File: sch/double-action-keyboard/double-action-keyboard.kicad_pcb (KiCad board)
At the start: 2 copper layers, 134 x 90 mm, 147 parts, among them J1 Conn_01x02, J2 Conn_01x04, J3 Conn_01x04, U1 Pico, U2 AQM1602XA-RN-GBW, U3 AQM1602Y-NLW-FBW

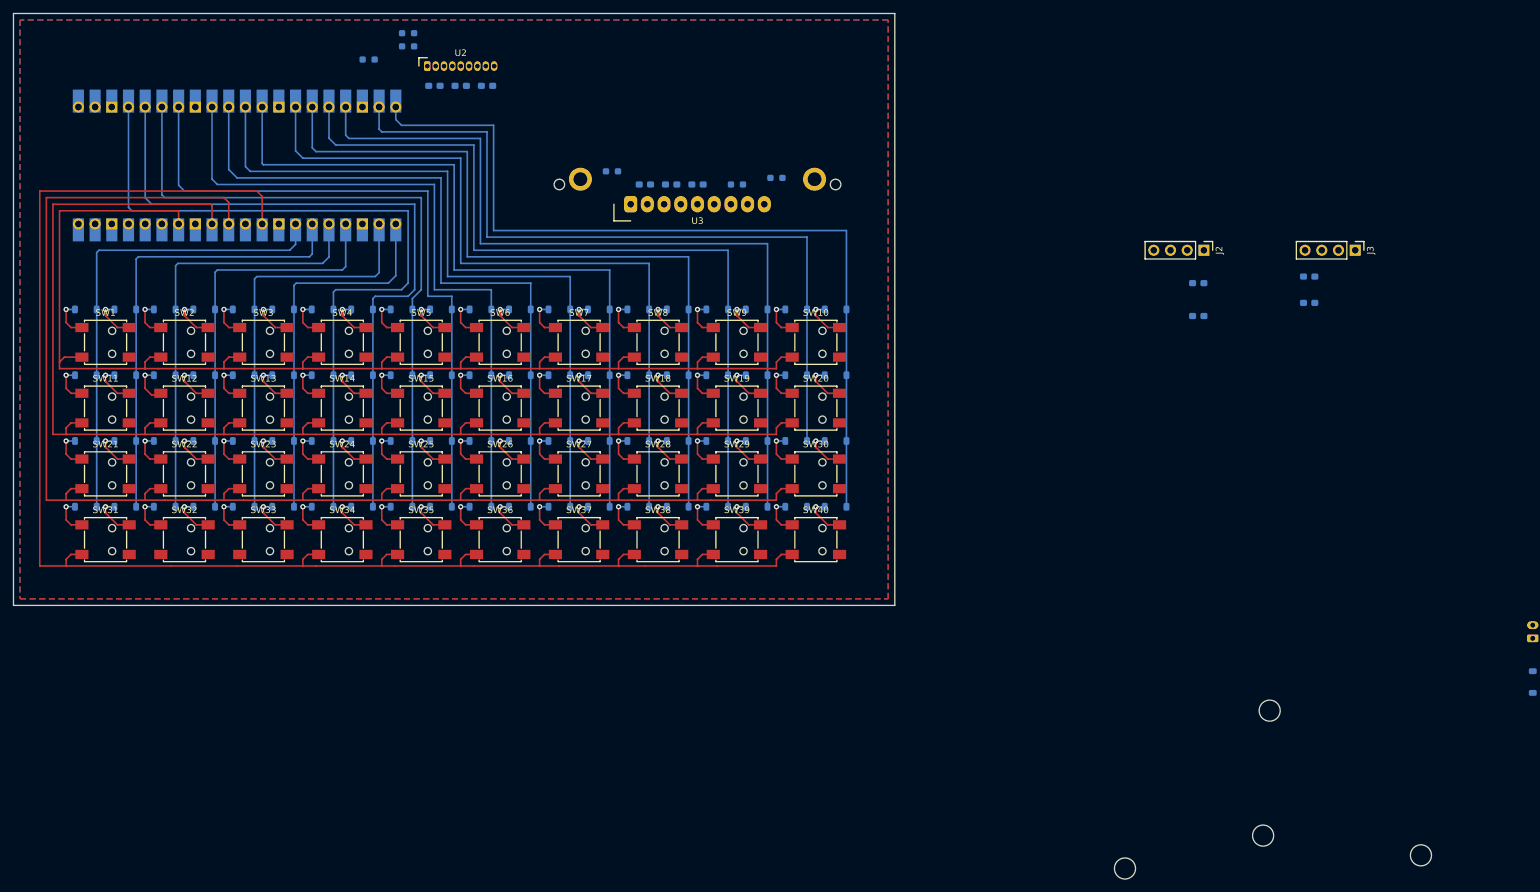
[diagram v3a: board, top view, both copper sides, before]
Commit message: picoの位置を右側に変更しました。
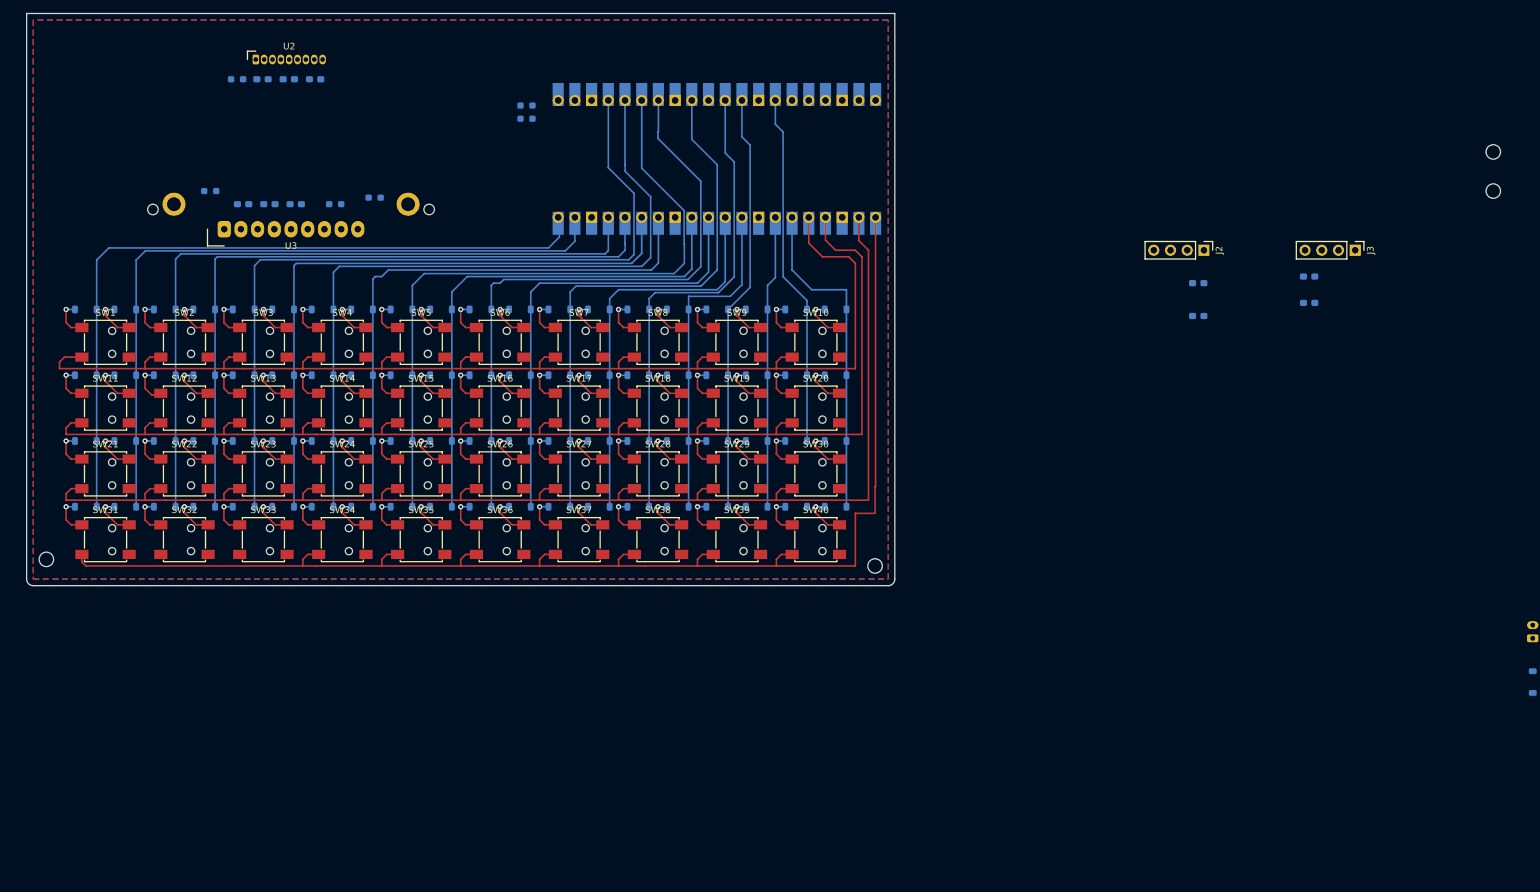
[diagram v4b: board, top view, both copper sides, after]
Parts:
- removed REF1 (x3), REF2: MountingHole_3.2mm_M3, MountingHole:MountingHole_3.2mm_M3
- added H1: MountingHole, MountingHole:MountingHole_2.2mm_M2, F.Cu at (51.0, 103.0)
- added H2: MountingHole, MountingHole:MountingHole_2.2mm_M2, F.Cu at (177.0, 104.0)
- added H3: MountingHole, MountingHole:MountingHole_2.2mm_M2, F.Cu at (271.0, 41.0)
- added H4: MountingHole, MountingHole:MountingHole_2.2mm_M2, F.Cu at (271.0, 47.0)
- moved U1 73.0 mm to (152.9, 42.1), turned to 90 degrees
- moved U3 61.9 mm to (88.2, 52.8)
- moved C4 61.2 mm to (88.9, 49.0)
- moved C5 61.2 mm to (80.9, 49.0)
- moved C6 61.2 mm to (84.9, 49.0)
- moved R4 61.2 mm to (75.9, 47.0)
- moved R5 61.2 mm to (100.9, 48.0)
- moved R6 61.2 mm to (94.9, 49.0)
- moved C1 26.2 mm to (83.9, 30.0)
- moved C2 26.2 mm to (87.9, 30.0)
- moved C3 26.2 mm to (91.9, 30.0)
- moved U2 26.1 mm to (87.9, 27.0)
- moved R1 21.1 mm to (124.0, 34.0)
- moved R2 21.1 mm to (124.0, 36.0)
- moved R3 20.2 mm to (80.0, 30.0)
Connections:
- U1 pad 1: /LCD_I2C_SDA -> /ROW3
- U1 pad 10: /COL11 -> /COL13
- U1 pad 11: /COL12 -> /COL11
- U1 pad 12: /COL13 -> /COL9
- U1 pad 14: /COL14 -> /COL7
- U1 pad 15: /COL15 -> /COL5
- U1 pad 16: /COL16 -> /COL3
- U1 pad 17: /COL17 -> /COL2
- U1 pad 19: /COL18 -> /COL1
- U1 pad 2: /LCD_I2C_SCL -> /ROW2
- U1 pad 20: /COL19 -> /COL0
- U1 pad 21: /COL5 -> /LCD_I2C_SDA
- U1 pad 22: /COL4 -> /LCD_I2C_SCL
- U1 pad 24: /COL3 -> /COL4
- U1 pad 25: /COL2 -> /COL6
- U1 pad 26: /COL1 -> /COL8
- U1 pad 27: /COL0 -> /COL10
- U1 pad 29: /ROW3 -> /COL12
- U1 pad 31: /ROW2 -> /COL14
- U1 pad 32: /ROW1 -> /COL16
- U1 pad 34: /ROW0 -> /COL18
- U1 pad 4: /COL6 -> /ROW1
- U1 pad 5: /COL7 -> /ROW0
- U1 pad 6: /COL8 -> /COL19
- U1 pad 7: /COL9 -> /COL17
- U1 pad 9: /COL10 -> /COL15
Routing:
- net /COL17: track 124.6 -> 44.5 mm
- net /COL19: track 128.8 -> 50.5 mm
- net /COL15: track 117.7 -> 51.1 mm
- net /COL18: track 115.6 -> 53.8 mm
- net /COL4: track 61.4 -> 120.1 mm
- net /COL16: track 120.9 -> 63.7 mm
- net /COL13: track 113.5 -> 60.1 mm
- net /COL2: track 65.5 -> 109.0 mm
- net /COL3: track 62.4 -> 105.6 mm
- net /COL14: track 113.9 -> 73.3 mm
- net /COL0: track 72.5 -> 112.4 mm
- net /COL1: track 69.3 -> 109.0 mm
- net /COL5: track 57.6 -> 95.8 mm
- net /COL11: track 106.0 -> 69.3 mm
- net /ROW3: track 237.0 -> 201.0 mm
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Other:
- board size 134 x 90 mm -> 132 x 87 mm

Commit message: ベタGNDにビアを打ちました。 空き領域にユニバーサル領域のスルーホールを追加しました。
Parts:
- added H5: MountingHole, MountingHole:MountingHole_2.2mm_M2, F.Cu at (51.0, 60.0)
- added H6: MountingHole, MountingHole:MountingHole_2.2mm_M2, F.Cu at (177.0, 60.0)
- J2, J3: footprint Connector_PinHeader_2.54mm:PinHeader_1x04_P2.54mm_Vertical -> OLED_I2C:OLED_I2C
- moved H3 220.6 mm to (51.0, 25.0)
- moved C8 157.3 mm to (71.1, 39.0)
- moved C7 156.3 mm to (71.1, 41.0)
- moved J2 150.7 mm to (77.6, 36.0)
- moved C9 146.7 mm to (98.1, 41.0)
- moved C10 146.4 mm to (98.1, 39.0)
- moved J3 146.4 mm to (105.0, 36.0)
- moved J1 144.5 mm to (164.0, 25.0), turned to 180 degrees
- moved D1 142.1 mm to (171.0, 27.0), turned to 180 degrees
- moved H4 96.5 mm to (177.0, 25.0)
- moved C1 7.99 mm to (89.1, 36.0), turned to 0 degrees
- moved R3 7.21 mm to (84.0, 36.0), turned to 180 degrees
- moved R4 5.22 mm to (71.1, 45.0)
- moved R6 5.18 mm to (100.1, 49.0), turned to 180 degrees
- moved R5 5.14 mm to (105.1, 45.0)
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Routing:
- net +3.3V: track 0.00 -> 176.9 mm, vias 0 -> 9
- net /LCD_I2C_SCL: track 0.00 -> 126.2 mm
- net /LCD_I2C_SDA: track 0.00 -> 122.1 mm
- net /COL18: track 53.8 -> 63.8 mm
- net /ROW3: track 201.0 -> 208.4 mm
- net /ROW0: track 187.4 -> 180.1 mm
- net Net-(D1-K): track 0.00 -> 7.00 mm
- net Net-(U2-RES_N): track 0.00 -> 6.44 mm, vias 0 -> 1
- net /ROW1: track 195.2 -> 188.8 mm
- net Net-(D1-A): track 0.00 -> 6.18 mm
- net /ROW2: track 202.7 -> 197.3 mm
- net Net-(U3-CAP1N): track 0.00 -> 4.39 mm
- net Net-(U3-RES_N): track 0.00 -> 4.34 mm
- net Net-(U3-LED_A): track 0.00 -> 4.29 mm
- net Net-(U3-VOUT): track 0.00 -> 4.22 mm
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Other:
- board size 132 x 87 mm -> 132 x 85 mm
- board text added: "double action keyboard v1.0 https://github.com/kenyahiro/double-action-keyboard"

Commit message: ステンシルの位置決め用穴を追加しました。
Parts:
- added REF**: hole1mm, hole1mm:hole1mm, F.Cu at (152.0, 27.0)
- added REF**: hole1mm, hole1mm:hole1mm, F.Cu at (53.0, 100.0)
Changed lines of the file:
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@@
+		)
+	)
+	(footprint "hole1mm:hole1mm"
+		(layer "F.Cu")
+		(at 152 27)
+		(property "Reference" "REF**"
+			(at 0 -0.5 0)
+			(unlocked yes)
+			(layer "F.SilkS")
+			(hide yes)
+			(effects
+				(font
+					(size 1 1)
+					(thickness 0.1)
+				)
+			)
+		)
+		(property "Value" "hole1mm"
+			(at 0 1 0)
+			(unlocked yes)
+			(layer "F.Fab")
+			(hide yes)
+			(effects
+				(font
+					(size 1 1)
+					(thickness 0.15)
+				)
+			)
+		)
+		(property "Footprint" "hole1mm:hole1mm"
+			(at 0 0 0)
+			(unlocked yes)
+			(layer "F.Fab")
+			(hide yes)
+			(effects
+				(font
+					(size 1 1)
+					(thickness 0.15)
+				)
+			)
+		)
+		(property "Datasheet" ""
+			(at 0 0 0)
+			(unlocked yes)
+			(layer "F.Fab")
+			(hide yes)
+			(effects
+				(font
+					(size 1 1)
+					(thickness 0.15)
+				)
+			)
+		)
+		(property "Description" ""
+			(at 0 0 0)
+			(unlocked yes)
+			(layer "F.Fab")
+			(hide yes)
+			(effects
+				(font
+					(size 1 1)
+					(thickness 0.15)
+				)
+			)
+		)
+		(attr smd)
+		(fp_text user "${REFERENCE}"
+			(at 0 2.5 0)
+			(unlocked yes)
+			(layer "F.Fab")
+			(hide yes)
+			(effects
+				(font
+					(size 1 1)
+					(thickness 0.15)
+				)
+			)
+		)
+		(pad "" np_thru_hole circle
+			(at 0 0)
+			(size 1 1)
+			(drill 1)
+			(layers "*.Mask" "F.Paste")
+			(solder_mask_margin 1)
 		)
 	)
@@
 		)
 	)
+	(footprint "hole1mm:hole1mm"
+		(layer "F.Cu")
+		(at 53 100)
+		(property "Reference" "REF**"
+			(at 0 -0.5 0)
+			(unlocked yes)
+			(layer "F.SilkS")
+			(hide yes)
+			(effects
+				(font
+					(size 1 1)
+					(thickness 0.1)
+				)
+			)
+		)
+		(property "Value" "hole1mm"
+			(at 0 1 0)
+			(unlocked yes)
+			(layer "F.Fab")
+			(hide yes)
+			(effects
+				(font
+					(size 1 1)
+					(thickness 0.15)
+				)
+			)
+		)
+		(property "Footprint" "hole1mm:hole1mm"
+			(at 0 0 0)
+			(unlocked yes)
+			(layer "F.Fab")
+			(hide yes)
+			(effects
+				(font
+					(size 1 1)
+					(thickness 0.15)
+				)
+			)
+		)
+		(property "Datasheet" ""
+			(at 0 0 0)
+			(unlocked yes)
+			(layer "F.Fab")
+			(hide yes)
+			(effects
+				(font
+					(size 1 1)
+					(thickness 0.15)
+				)
+			)
+		)
+		(property "Description" ""
+			(at 0 0 0)
+			(unlocked yes)
+			(layer "F.Fab")
+			(hide yes)
+			(effects
+				(font
+					(size 1 1)
+					(thickness 0.15)
+				)
+			)
+		)
+		(attr smd)
+		(fp_text user "${REFERENCE}"
+			(at 0 2.5 0)
+			(unlocked yes)
+			(layer "F.Fab")
+			(hide yes)
+			(effects
+				(font
+					(size 1 1)
+					(thickness 0.15)
+				)
+			)
+		)
+		(pad "" np_thru_hole circle
+			(at 0 0)
+			(size 1 1)
+			(drill 1)
+			(layers "*.Mask" "F.Paste")
+			(solder_mask_margin 1)
+		)
+	)
